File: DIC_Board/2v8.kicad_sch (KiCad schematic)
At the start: 8 parts, among them J30 0430450200, U30 TPS27S100APWPR

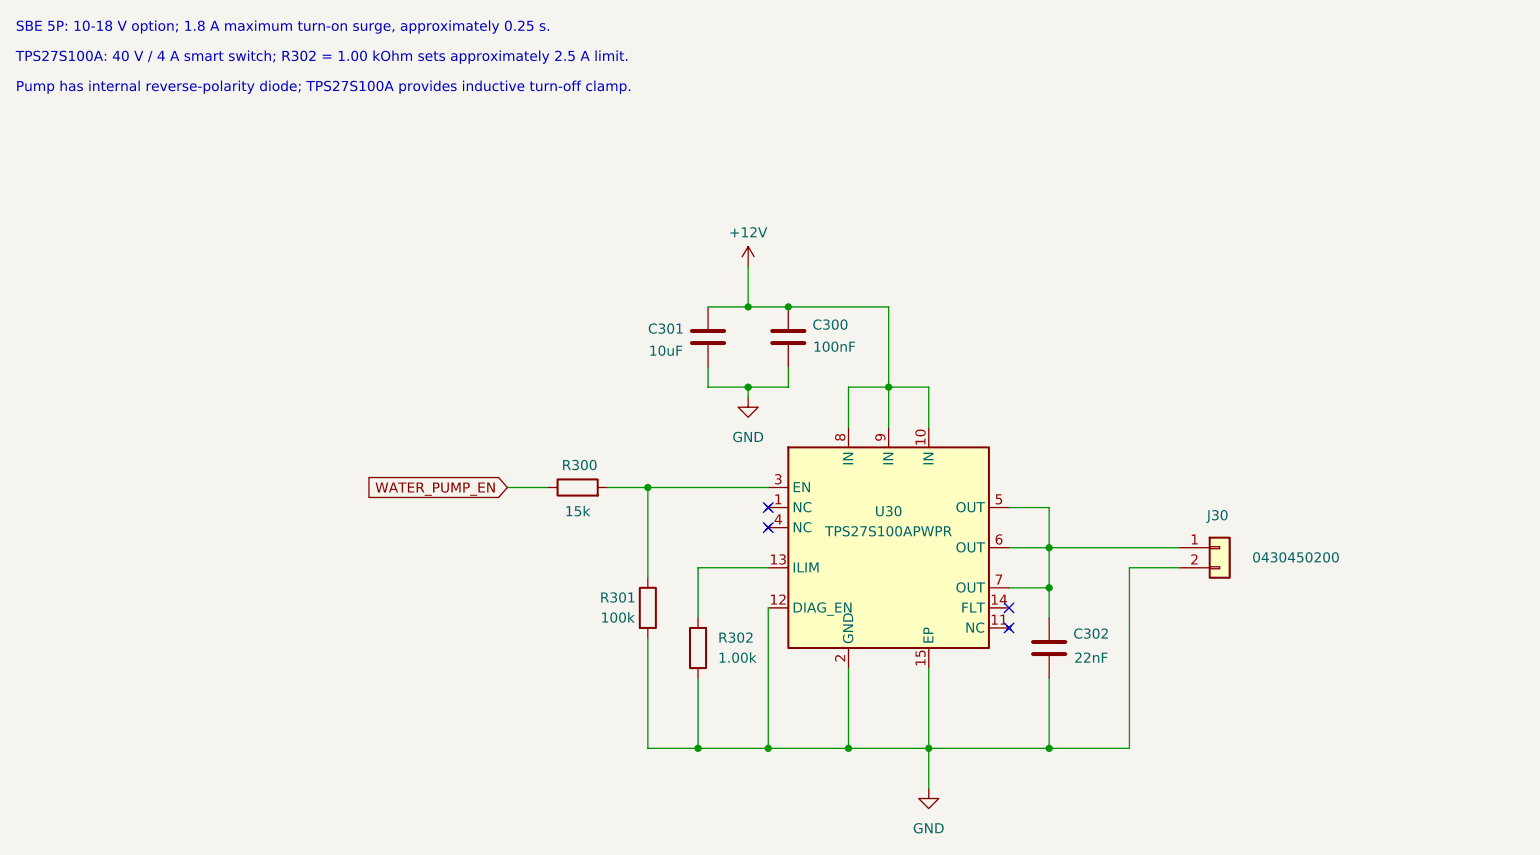
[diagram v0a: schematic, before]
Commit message: Separated the power sheets, did the sensor sheets.
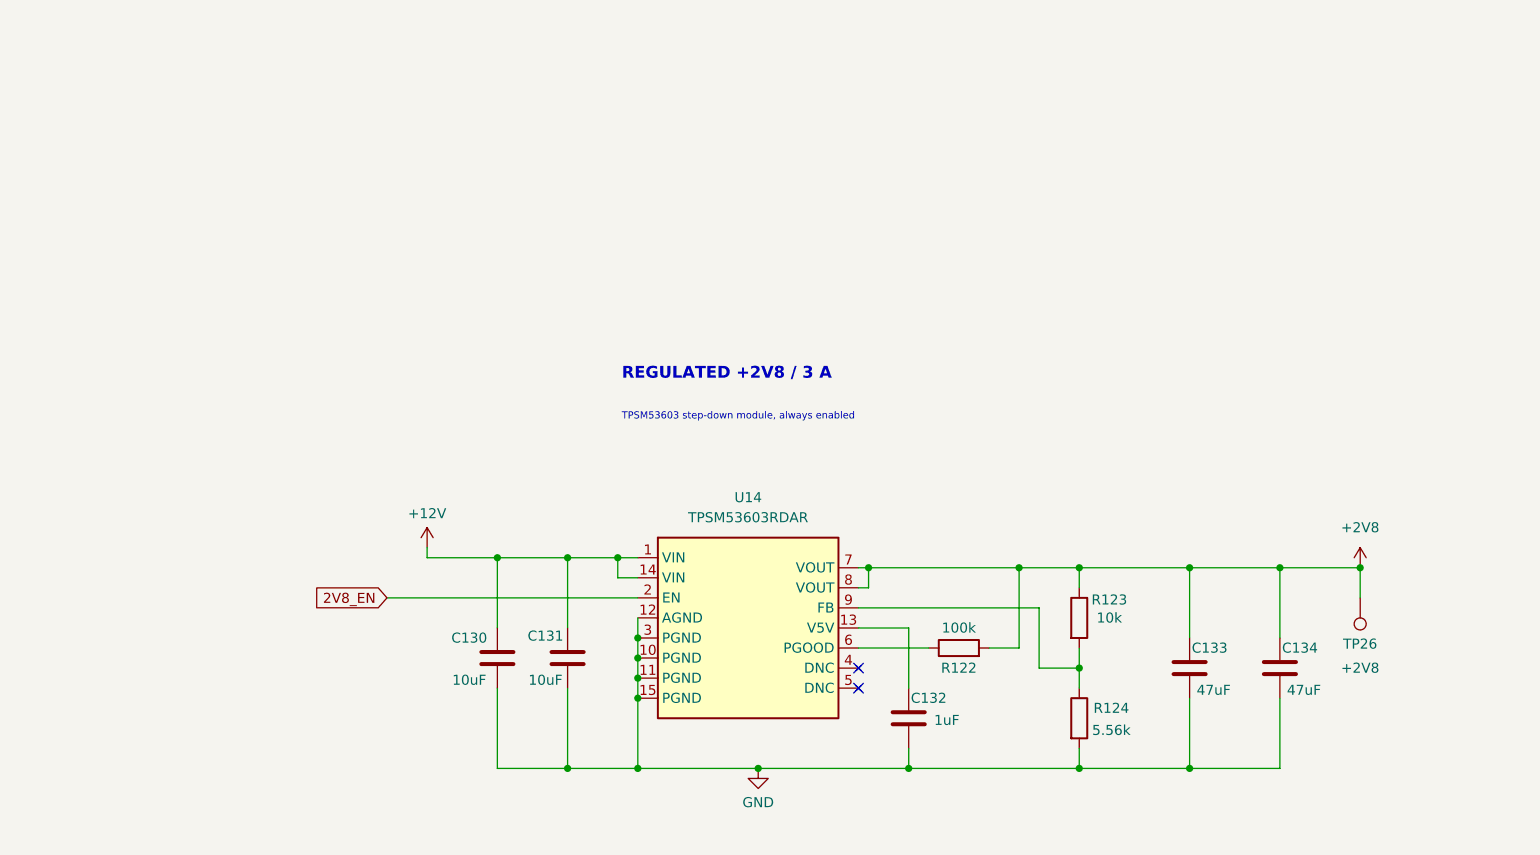
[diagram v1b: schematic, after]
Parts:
- removed C300: 100nF, Capacitor_SMD:C_0402_1005Metric, symbol Device:C
- removed C301: 10uF, Capacitor_SMD:C_1206_3216Metric, symbol Device:C
- removed C302: 22nF, Capacitor_SMD:C_0402_1005Metric, symbol Device:C
- removed J30: 0430450200, Connector_Molex:Molex_Micro-Fit_3.0_43045-0200_2x01_P3.00mm_Horizontal, symbol Connector_Generic:Conn_01x02
- removed R300: 15k, Resistor_SMD:R_0402_1005Metric, symbol Device:R
- removed R301: 100k, Resistor_SMD:R_0402_1005Metric, symbol Device:R
- removed R302: 1.00k, Resistor_SMD:R_0402_1005Metric, symbol Device:R
- removed U30: TPS27S100APWPR, Package_SO:Texas_HTSSOP-14-1EP_4.4x5mm_P0.65mm_EP3.4x5mm_Mask3.155x3.255mm_ThermalVias, symbol DIC_Board:TPS27S100A
- added C130, C131: 10uF, Capacitor_SMD:C_1206_3216Metric, symbol Device:C
- added C132: 1uF, Capacitor_SMD:C_0603_1608Metric, symbol Device:C
- added C133, C134: 47uF, Capacitor_SMD:C_1210_3225Metric, symbol Device:C
- added R122: 100k, Resistor_SMD:R_0402_1005Metric, symbol Device:R
- added R123: 10k, Resistor_SMD:R_0402_1005Metric, symbol Device:R
- added R124: 5.56k, Resistor_SMD:R_0402_1005Metric, symbol Device:R
- added TP26: +2V8, TestPoint:TestPoint_Plated_Hole_D2.0mm, symbol Connector:TestPoint
- added U14: TPSM53603RDAR, Package_DFN_QFN:Texas_B3QFN-14-1EP_5x5.5mm_P0.65mm_ThermalVia, symbol DIC_Board:TPSM53603RDA
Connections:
- net +12V: now also C130.1, C131.1, U14.1 (VIN), U14.14 (VIN)
- net GND: now also C130.2, C131.2, C132.2, C133.2, C134.2, R124.2, U14.10 (PGND), U14.11 (PGND), U14.12 (AGND), U14.15 (PGND), U14.3 (PGND)
- new net: R123.2, R124.1, U14.9 (FB)
- new net: C132.1, U14.13 (V5V)
- new net: R122.1, U14.6 (PGOOD)
- new net +2V8: C133.1, C134.1, R122.2, R123.1, TP26.1, U14.7 (VOUT), U14.8 (VOUT)
- new net 2V8_EN: U14.2 (EN)
- no-connect marks 4 -> 2
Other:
- note added: "REGULATED +2V8 / 3 A"
- note added: "TPSM53603 step-down module, always enabled"
- note removed: "Pump has internal reverse-polarity diode; TPS27S100A provides inductive turn-off clamp."
- note removed: "SBE 5P: 10-18 V option; 1.8 A maximum turn-on surge, approximately 0.25 s."
- note removed: "TPS27S100A: 40 V / 4 A smart switch; R302 = 1.00 kOhm sets approximately 2.5 A limit."
- title: Water Pump -> (none)

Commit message: Synchronize schematic hierarchy and MCU pin map
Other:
- note added: "TPSM53603 step-down module; default-on, MCU-controllable"
- note removed: "TPSM53603 step-down module, always enabled"
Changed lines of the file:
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@@
 		)
 	)
-	(text "TPSM53603 step-down module, always enabled"
+	(text "TPSM53603 step-down module; default-on, MCU-controllable"
 		(exclude_from_sim no)
 		(at 105.918 72.898 0)
@@
 		)
 	)
-	(global_label "2V8_EN"
+	(hierarchical_label "2V8_EN"
 		(shape input)
 		(at 76.2 95.25 180)
-		(fields_autoplaced yes)
 		(effects
 			(font
@@
 			(justify right)
 		)
-		(property "Intersheetrefs" "${INTERSHEET_REFS}"
-			(at 66.2601 95.25 0)
-			(hide yes)
-			(show_name no)
-			(do_not_autoplace no)
-			(effects
-				(font
-					(size 1.27 1.27)
-				)
-				(justify right)
-			)
-		)
-	)
+	)

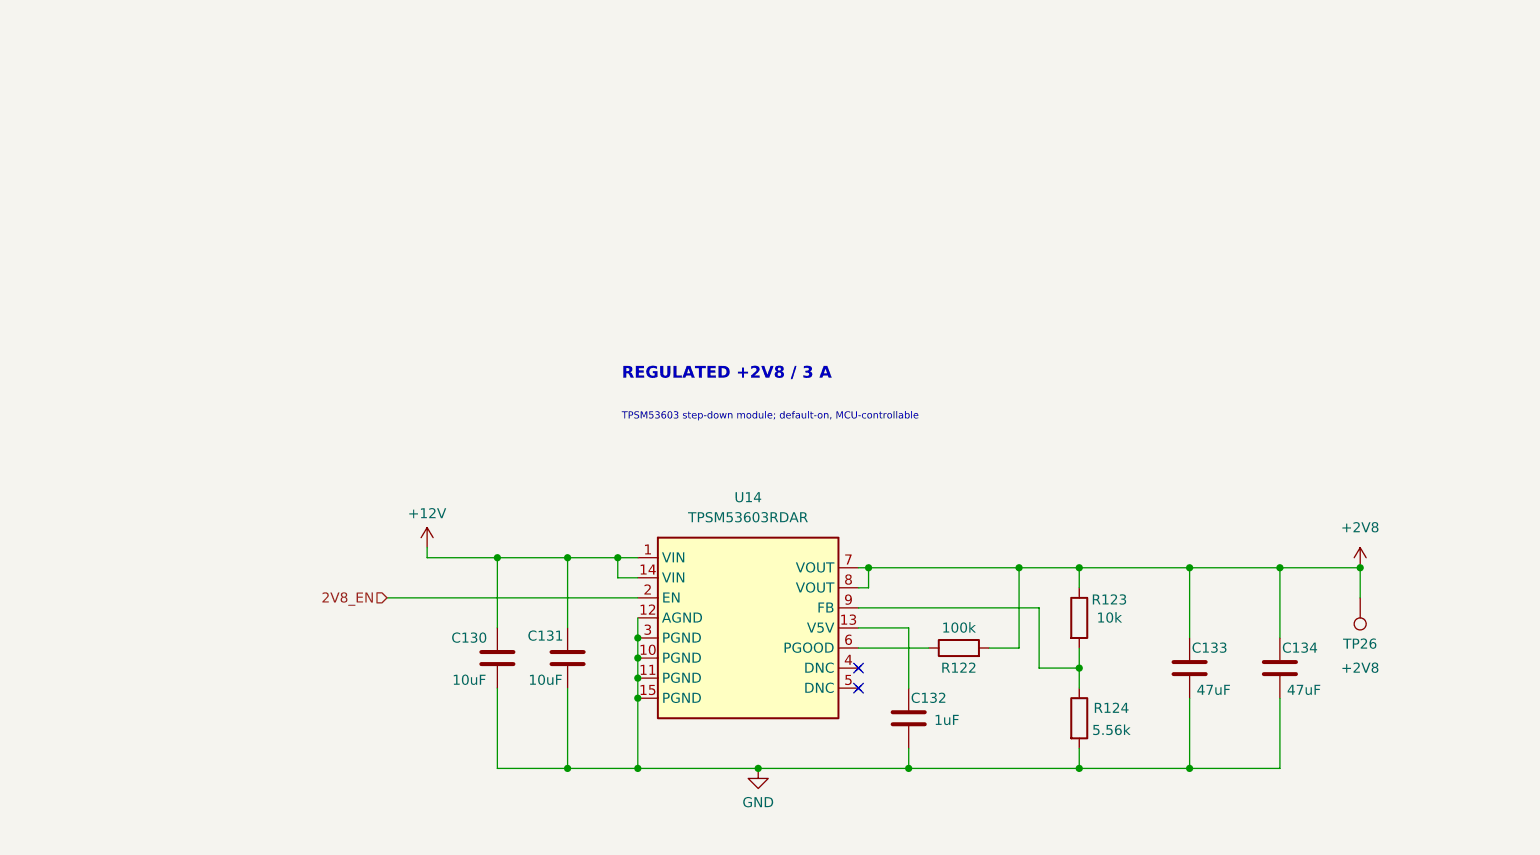
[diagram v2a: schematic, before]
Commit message: Synchronize power, communications, and MCU configuration
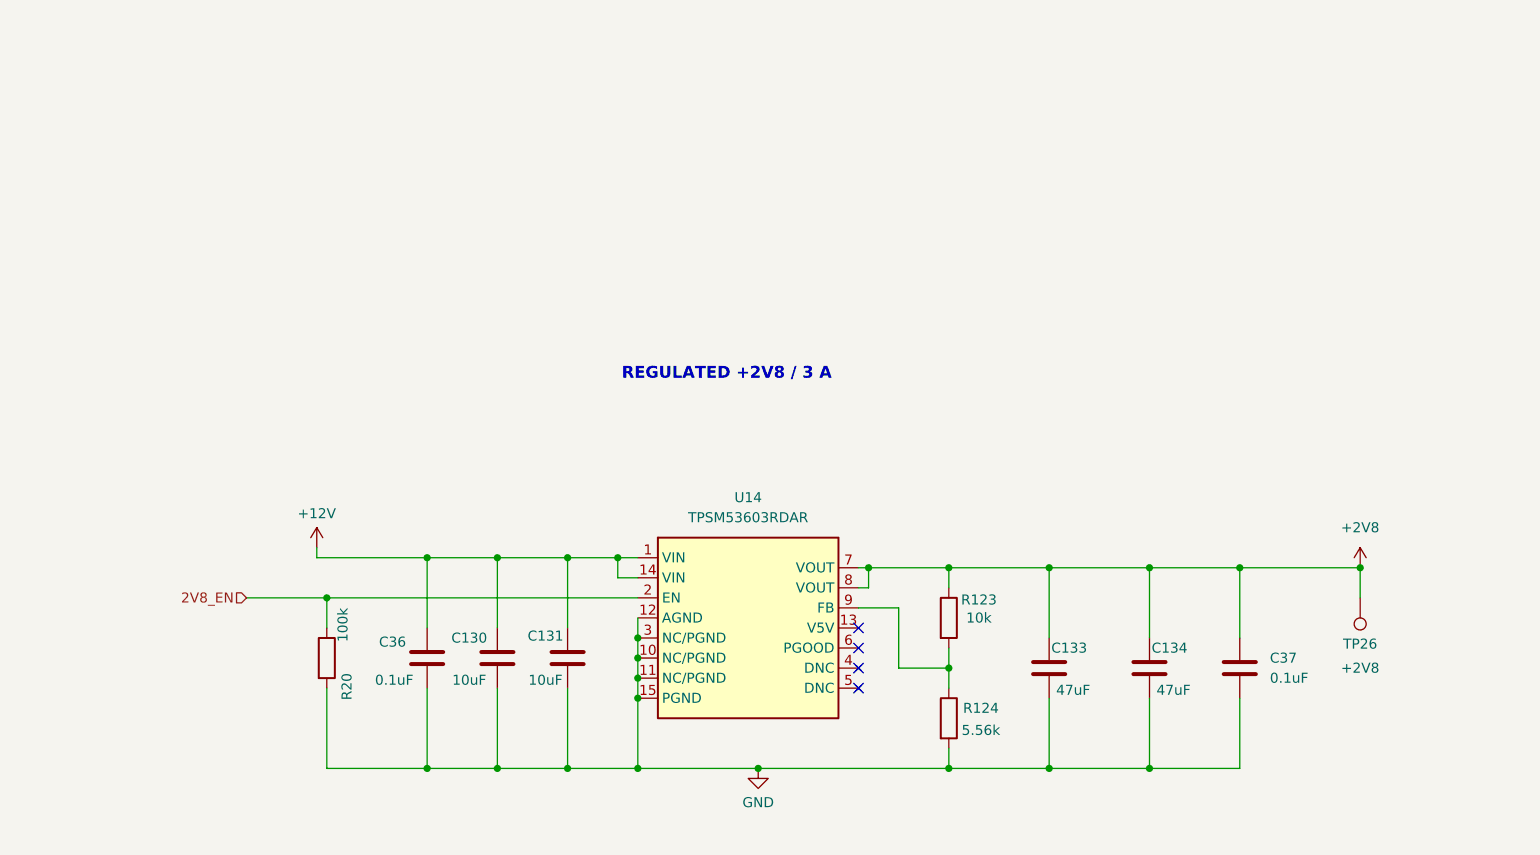
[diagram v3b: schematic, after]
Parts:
- removed C132: 1uF, Capacitor_SMD:C_0603_1608Metric, symbol Device:C
- removed R122: 100k, Resistor_SMD:R_0402_1005Metric, symbol Device:R
- added C36, C37: 0.1uF, symbol Device:C
- added R20: 100k, Resistor_SMD:R_0402_1005Metric, symbol Device:R
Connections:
- net +12V: now also C36.1
- net +2V8: now also C37.1
- net 2V8_EN: now also R20.1
- net GND: now also C36.2, C37.2, R20.2
- no-connect marks 2 -> 4
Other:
- note removed: "TPSM53603 step-down module; default-on, MCU-controllable"
- moved on the sheet: C133, C134, R123, R124

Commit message: Updated board for layout! All footprints added
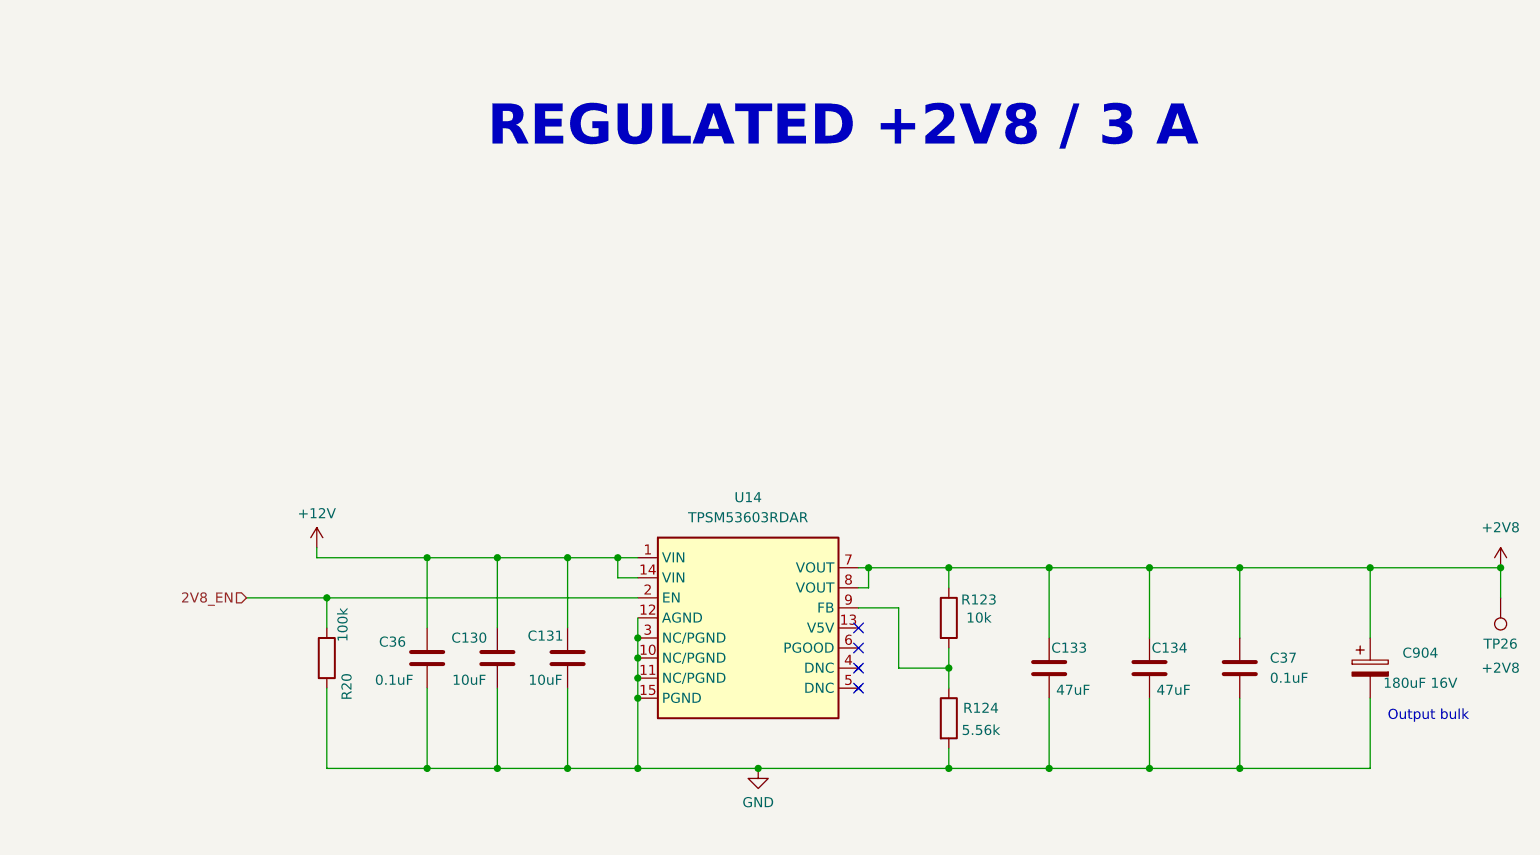
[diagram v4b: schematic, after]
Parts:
- added C904: 180uF 16V, Capacitor_SMD:CP_Elec_6.3x5.9, symbol Device:C_Polarized
- C36, C37: footprint (none) -> Capacitor_SMD:C_0603_1608Metric; BOM Source (none) -> https://product.tdk.com/en/search/capacitor/ceramic/mlcc/in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; Dielectric (none) -> X7R; MPN (none) -> C1608X7R1H104K080AA; Manufacturer (none) -> TDK; Tolerance (none) -> 10%; Voltage Rating (none) -> 50V
- TP26: now left out of the parts list
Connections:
- net +2V8: now also C904.1
- net GND: now also C904.2
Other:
- note added: "Output bulk"
- moved on the sheet: TP26

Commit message: Preliminary layout
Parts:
- TP26: footprint TestPoint:TestPoint_Plated_Hole_D2.0mm -> TestPoint:TestPoint_Pad_D1.0mm
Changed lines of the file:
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@@
 			)
 		)
-		(property "Footprint" "TestPoint:TestPoint_Plated_Hole_D2.0mm"
+		(property "Footprint" "TestPoint:TestPoint_Pad_D1.0mm"
 			(at 217.17 95.25 0)
 			(hide yes)
